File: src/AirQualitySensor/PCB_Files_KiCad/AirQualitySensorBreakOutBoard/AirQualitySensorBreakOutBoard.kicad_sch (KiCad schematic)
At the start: 19 parts, among them J1 Conn_01x02_Male, J2 Conn_01x02_Male, J3 Conn_01x02_Male, J4 Conn_01x07_Male, Q1 IRLB8721PBF, U1 PMS5003, U2 PMS5003, U3 SPS30, U4 SHT31, U5 Boost_Converter, U6 lilygo-ttgo-t-sim7000g-esp32-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, U7 Buck/Boost_Converter

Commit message: Merged AQS
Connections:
- net VDD_EN: now also U6.12; no longer U6.13
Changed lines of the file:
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@@
     )
   )
-  (global_label "VDD_EN" (shape input) (at 203.2 120.65 180) (fields_autoplaced)
+  (global_label "VDD_EN" (shape input) (at 203.2 125.73 180) (fields_autoplaced)
     (effects (font (size 1.27 1.27)) (justify right))
-    (property "Intersheet References" "${INTERSHEET_REFS}" (id 0) (at 193.7112 120.5706 0)
+    (property "Intersheet References" "${INTERSHEET_REFS}" (id 0) (at 193.7112 125.6506 0)
       (effects (font (size 1.27 1.27)) (justify right) hide)
     )

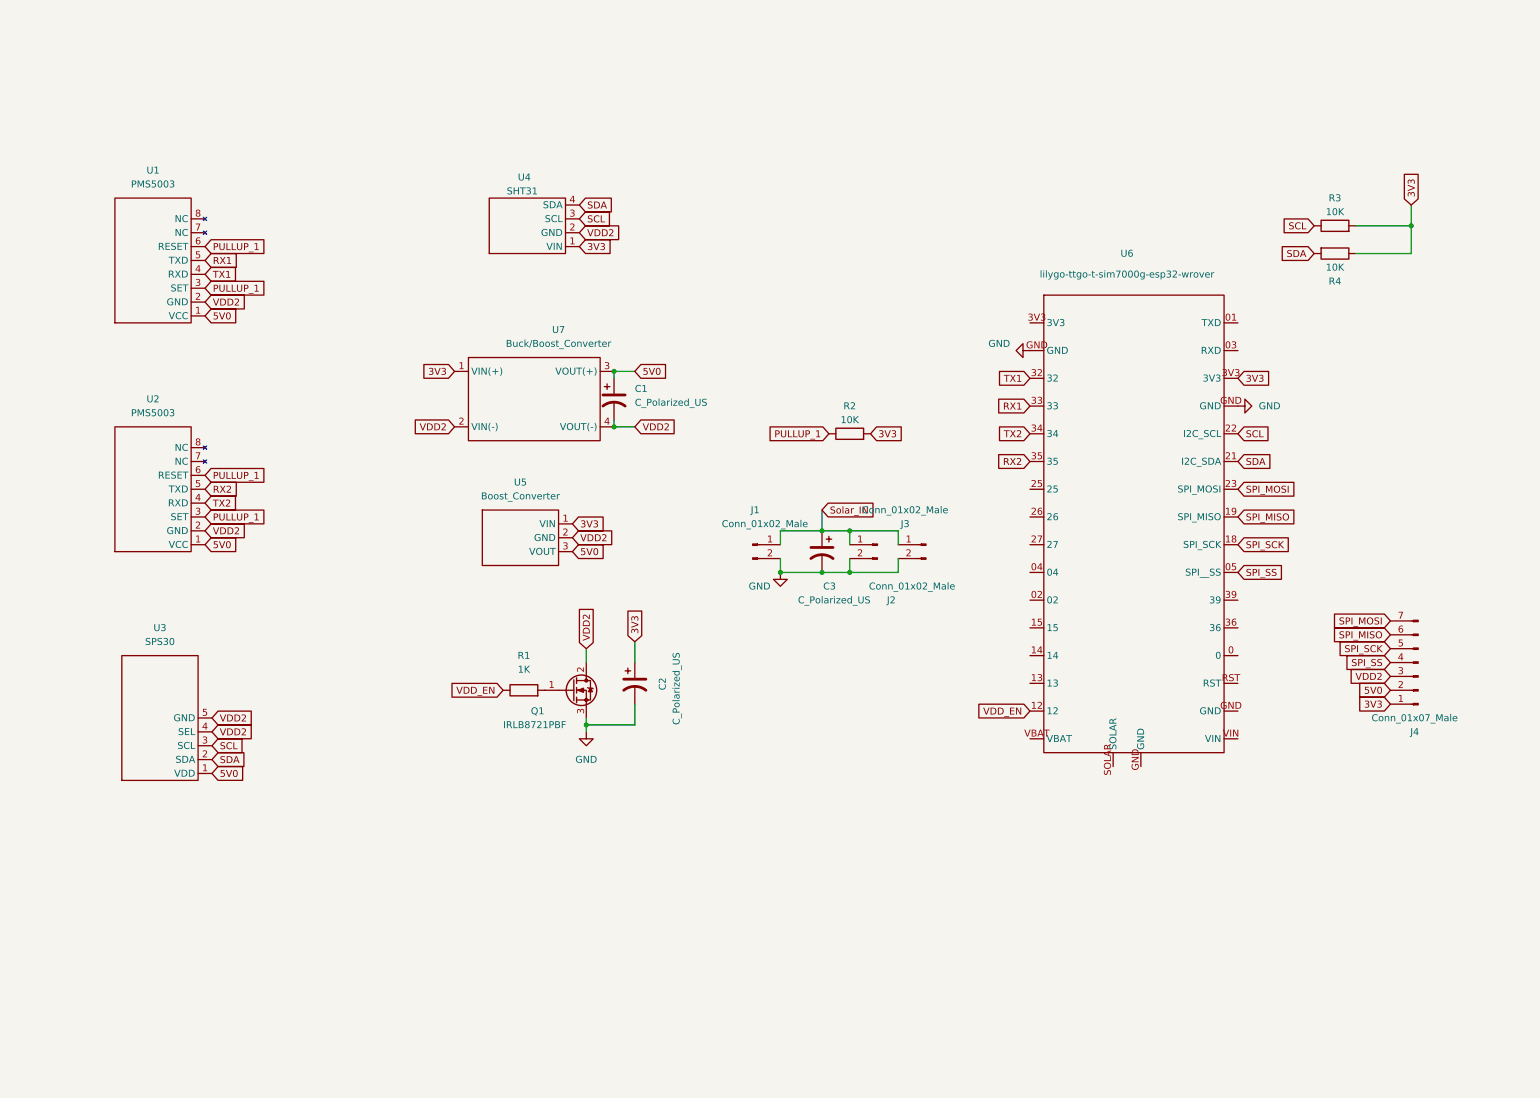
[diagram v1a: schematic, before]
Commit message: Updated doc Fritzing file AQS and PCB KiCad
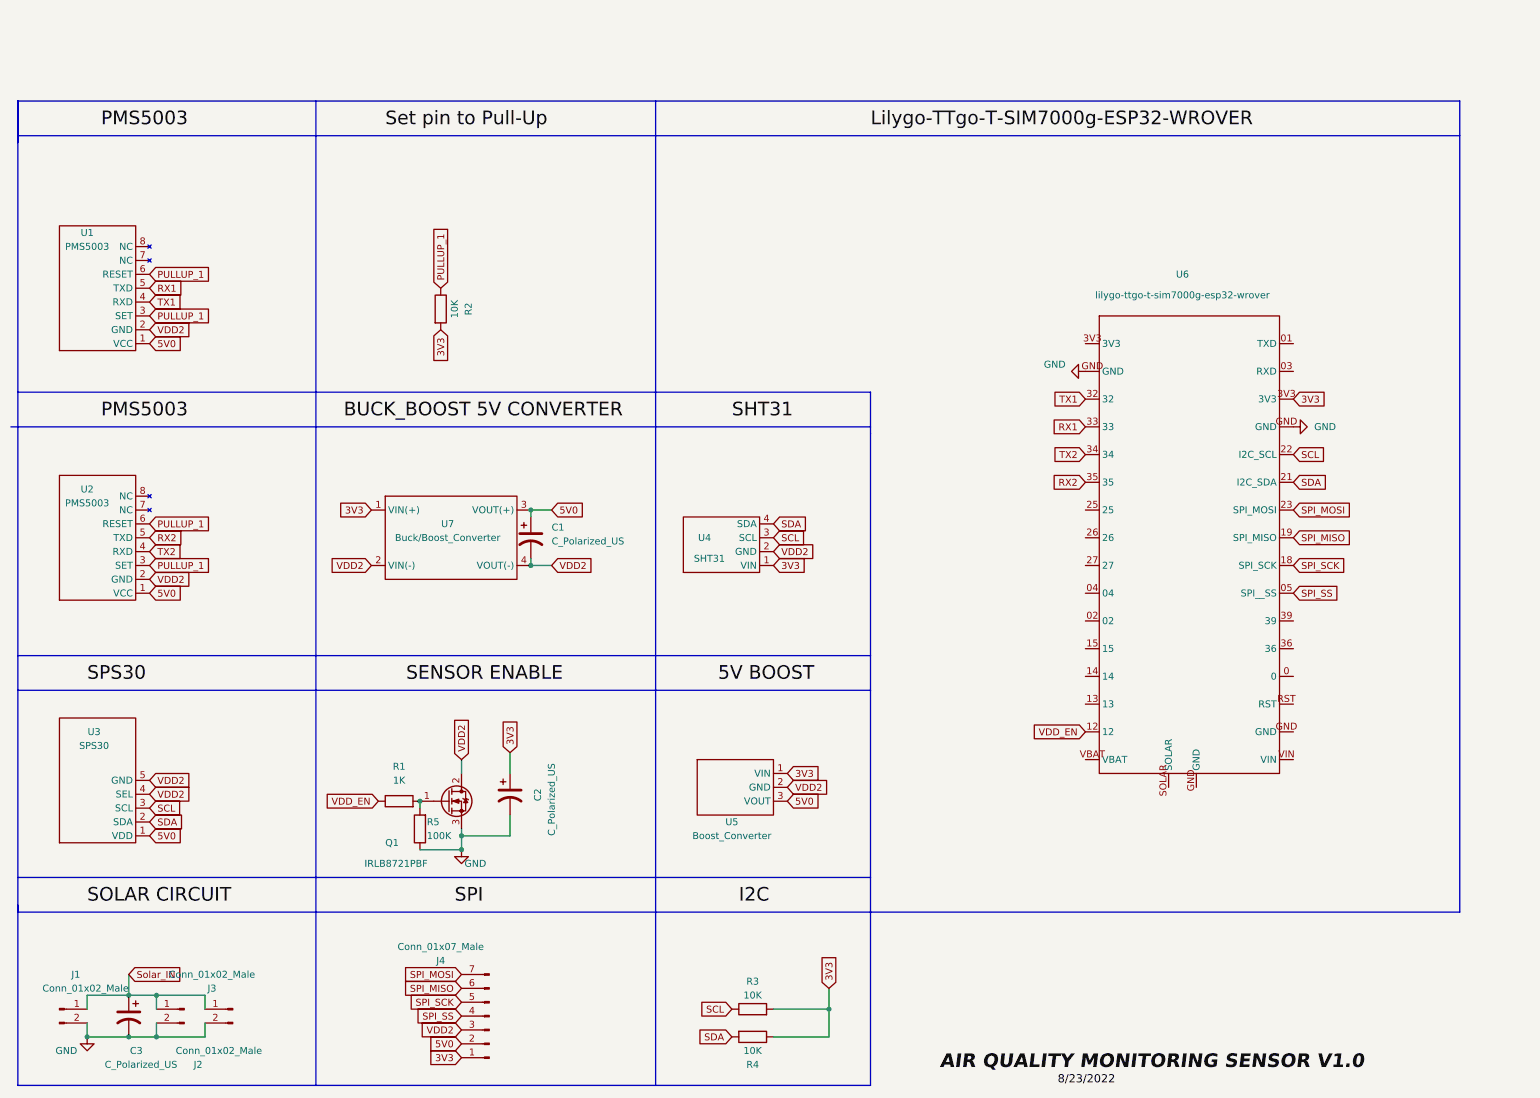
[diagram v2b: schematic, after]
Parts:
- added R5: 100K, Resistor_THT:R_Axial_DIN0204_L3.6mm_D1.6mm_P7.62mm_Horizontal, symbol Device:R
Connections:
- net GND: now also R5.1
- net at Q1.1 (G), R1.2: now also R5.2
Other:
- moved on the sheet: C1, C2, C3, J1, J2, J3, J4, Q1, R1, R2, R3, R4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
